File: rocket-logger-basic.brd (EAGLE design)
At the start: 58.5 x 62 mm, 63 parts, among them IC1 CC430F513X, U1 MAX1555, X1 0896BM15A0001, X2 USB-MICROB, X3 SMA-142-0701-801/806

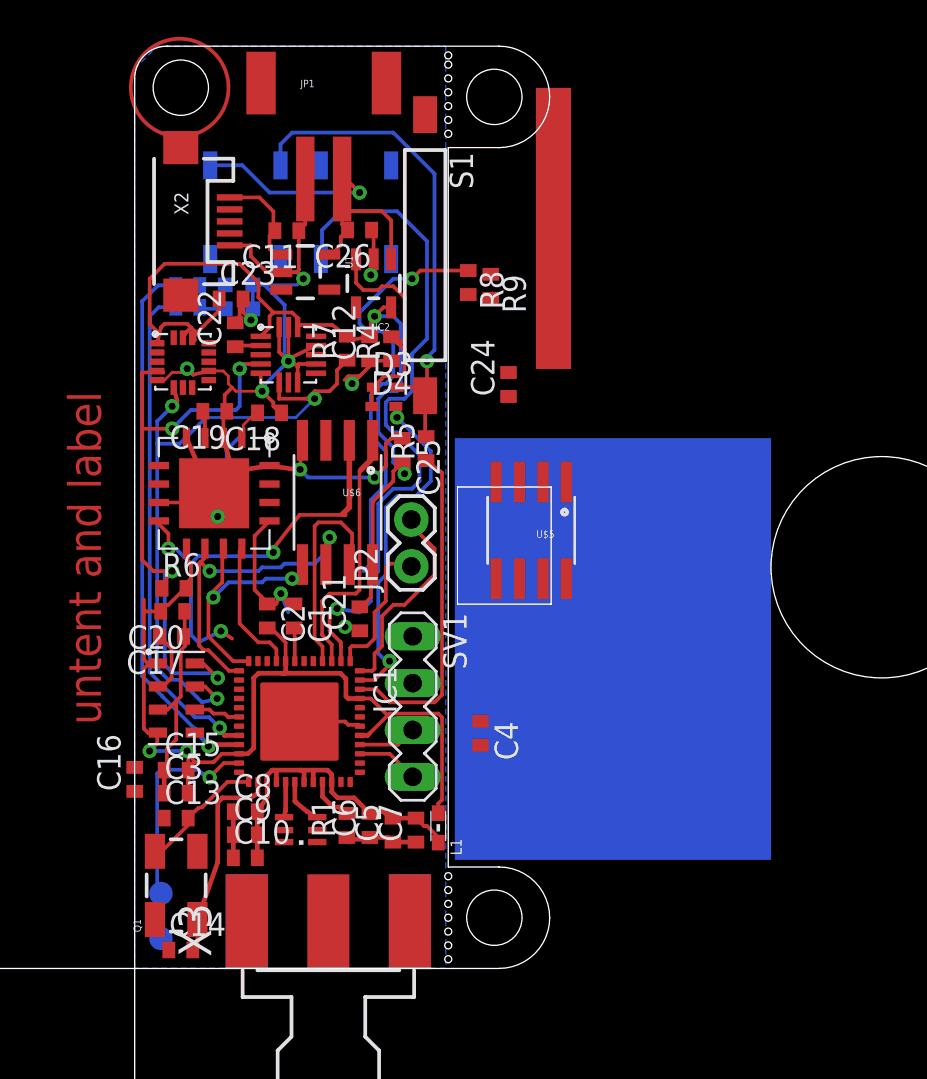
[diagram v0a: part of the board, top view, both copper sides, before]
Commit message: added mini logger
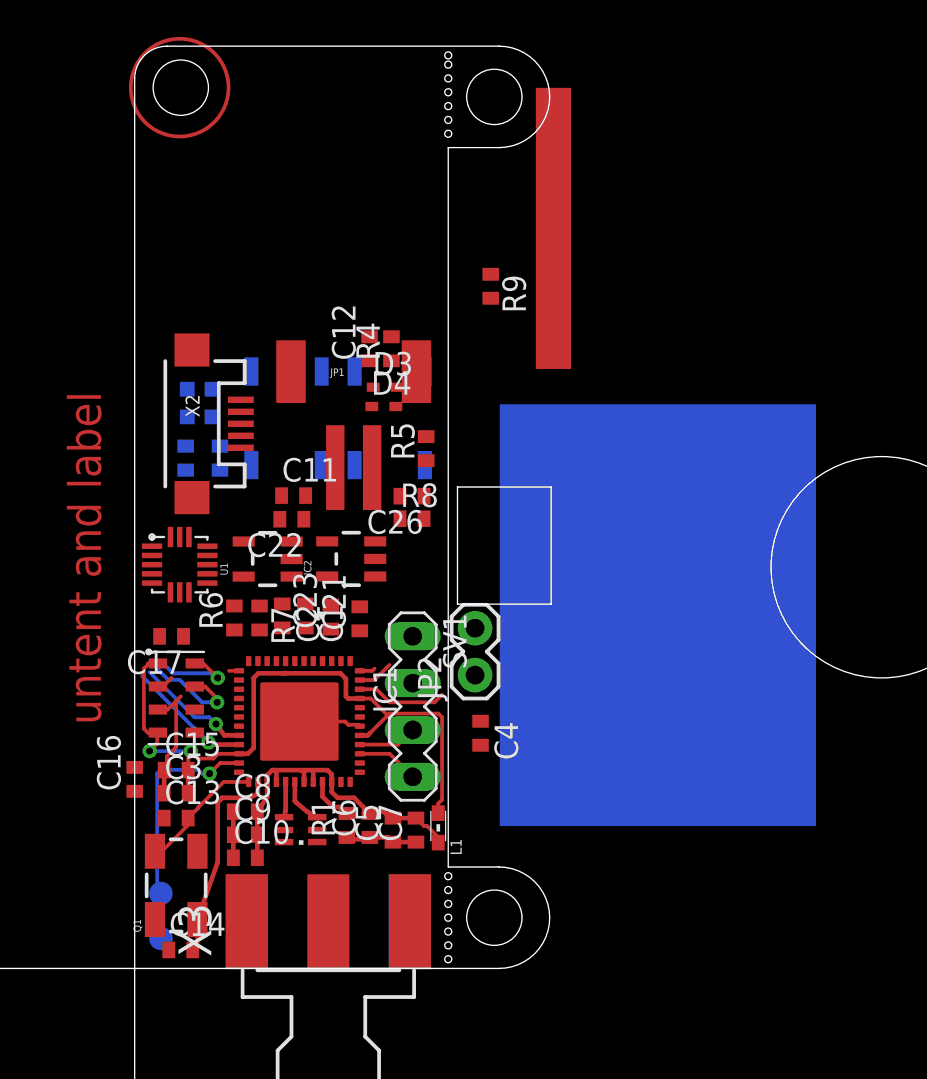
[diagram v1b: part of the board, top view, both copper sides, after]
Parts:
- removed C18, C19: 1u, resistor:C0402
- removed C20: 100n, resistor:C0402
- removed C24, C25: (no value), resistor:C0402
- removed S1: REED-SWITCH-CT10-1530-G1, switch-reed:CT10-G1
- removed U$1: MAX21000, Mine:LGA16
- removed U$2: MMA68XX, Mine:QFN16-6X6
- removed U$5: SPI_FLASH-X25XXSMD, SparkFun:SO08
- removed U$6: SPI_FLASH-X25XXSMD1, SparkFun:SO08-EIAJ
- moved C23 18.1 mm to (10.6, 19.0), turned to 90 degrees
- moved JP1 15.7 mm to (11.9, 30.9)
- moved U1 15.7 mm to (7.21, 22.2), turned to 90 degrees
- moved R7 15.4 mm to (6.77, 19.0), turned to 270 degrees
- moved IC2 15.0 mm to (11.7, 22.2), turned to 90 degrees
- moved C26 14.7 mm to (15.0, 25.6)
- moved C11 14.4 mm to (8.62, 25.6), turned to 0 degrees
- moved R8 13.2 mm to (15.0, 24.4), turned to 0 degrees
- moved U$3 12.8 mm to (2.44, 21.9)
- moved S2 11.4 mm to (8.24, 29.8)
- moved S4 11.3 mm to (13.8, 29.8)
- moved X2 11.0 mm to (3.11, 29.5)
- moved C22 10.5 mm to (8.52, 24.4), turned to 180 degrees
- moved R2 9.53 mm to (4.62, 27.7), turned to 90 degrees
- moved R3 8.18 mm to (2.76, 27.7), turned to 90 degrees
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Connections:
- removed net DSYNC: U$1.12
- removed net N$14: C18.2, U$2.1
- removed net N$15: C19.2, U$2.3
- removed net N$27: U$6.3
- removed net P_INT: IC1.18, U$4.6
- net +3V3: no longer C20.2, C24.2, C25.2, U$1.1, U$1.14, U$1.15, U$2.9, U$6.8
- net CLK: no longer U$2.10, U$6.6
- net CS: no longer U$2.12
- net CS_F: no longer U$6.1
- net GND: no longer C18.1, C19.1, C20.1, C24.1, C25.1, U$1.10, U$1.5, U$1.7, U$2.13, U$2.16, U$2.17, U$2.2, U$2.4, U$2.7, U$3.7, U$6.4
- net HOLD: no longer U$6.7
- net MISO: no longer U$2.8, U$6.2
- net MOSI: no longer U$2.11, U$6.5
- net N$2: no longer S1.1
- net N$24: no longer S1.2
- net SCL: no longer U$1.4
- net SDA: no longer U$1.6
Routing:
- net GND: track 113.1 -> 17.0 mm, vias 12 -> 0
- net +3V3: track 100.6 -> 38.4 mm, vias 4 -> 2
- net N$2: track 43.2 -> 0.00 mm, vias 2 -> 0
- net N$28: track 37.3 -> 0.00 mm, vias 1 -> 0
- net SDA: track 38.0 -> 5.69 mm, vias 3 -> 1
- net SCL: track 34.2 -> 4.88 mm, vias 4 -> 1
- net N$24: track 26.8 -> 0.00 mm, vias 1 -> 0
- net MISO: track 23.9 -> 0.00 mm, vias 3 -> 0
- net N$16: track 29.4 -> 6.79 mm
- net N$17: track 27.2 -> 6.31 mm
- net CLK: track 17.9 -> 0.54 mm, vias 2 -> 0
- net KEEPON: track 19.1 -> 1.95 mm, vias 2 -> 0
- net CS_F: track 14.2 -> 0.00 mm
- net MOSI: track 14.2 -> 0.00 mm, vias 2 -> 0
- net SWITCHON: track 18.0 -> 4.92 mm
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- removed copper zone on layer 16, net GND

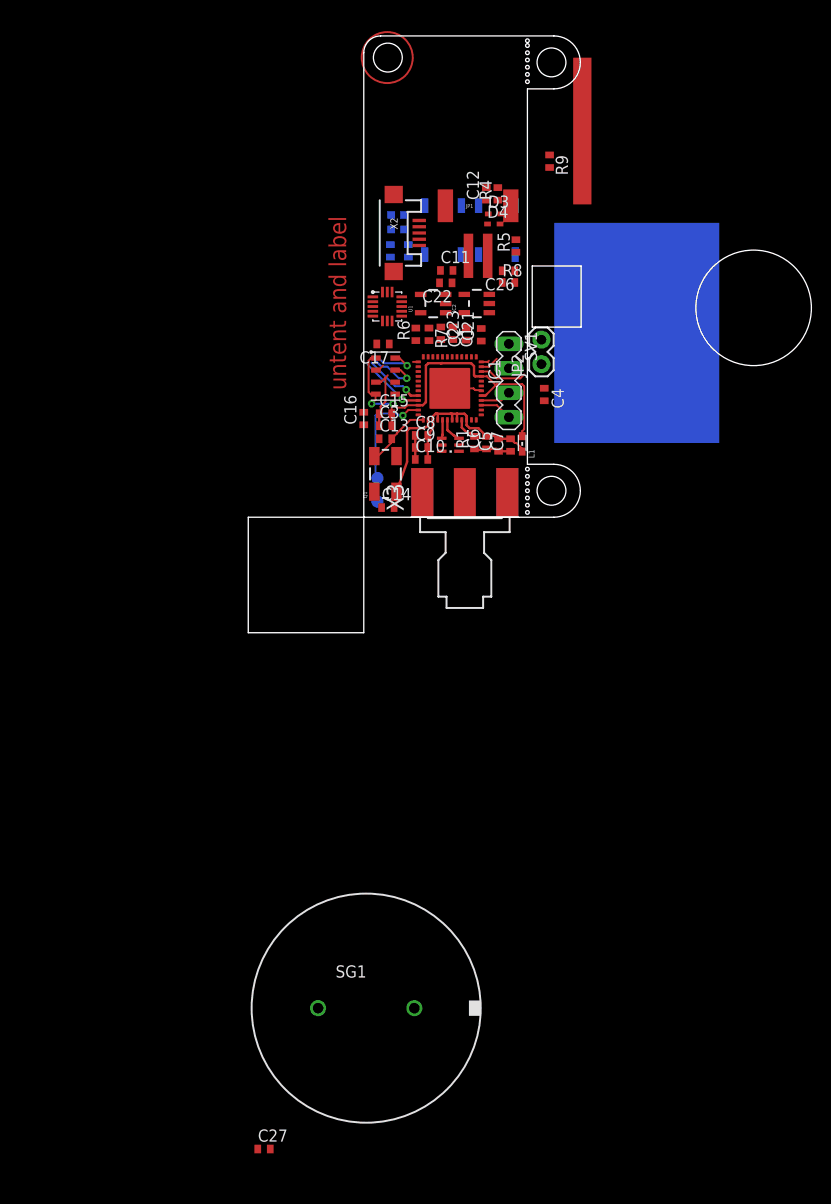
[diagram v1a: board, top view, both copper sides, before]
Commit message: removed accel from simple verison, done some routing on main one
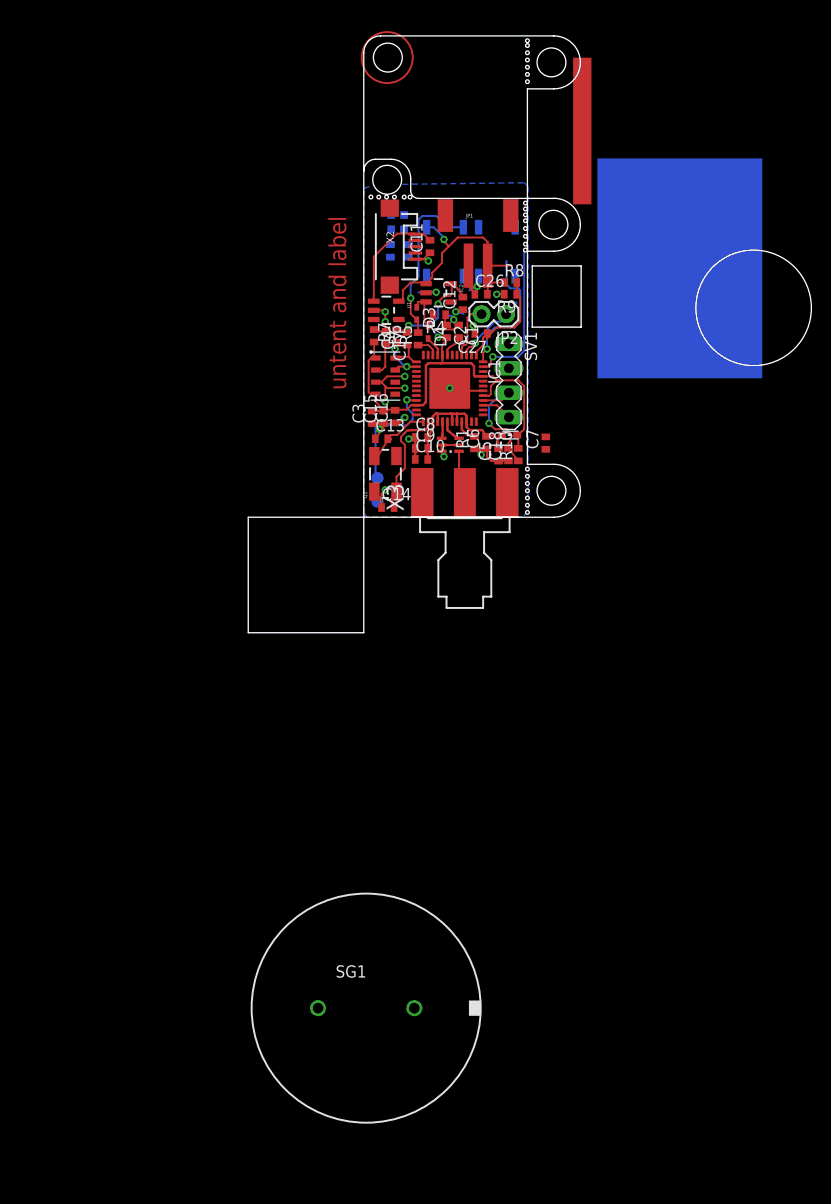
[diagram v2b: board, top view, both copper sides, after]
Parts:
- removed C21: 4.7u, resistor:C0402
- removed C22, C23: 100n, resistor:C0402
- removed U$3: MMA8452Q, Mine:QFN16-COL
- added C18: (no value), resistor:C0402
- added R10: (no value), rcl:R0402
- moved C27 87.7 mm to (12.2, 19.1), turned to 180 degrees
- moved C4 18.7 mm to (1.07, 18.8)
- moved R9 14.4 mm to (15.2, 23.2), turned to 180 degrees
- moved R5 14.0 mm to (5.64, 18.5)
- moved R4 13.9 mm to (7.86, 21.0), turned to 180 degrees
- moved D4 13.1 mm to (6.69, 19.3), turned to 270 degrees
- moved D3 13.1 mm to (5.50, 21.2), turned to 270 degrees
- moved C12 11.6 mm to (10.3, 22.2)
- moved JP2 6.36 mm to (14.8, 21.1), turned to 180 degrees
- moved U1 4.92 mm to (2.34, 21.5), turned to 270 degrees
- moved IC2 4.13 mm to (7.77, 23.3), turned to 270 degrees
- moved C26 3.75 mm to (12.2, 23.2), turned to 0 degrees
- moved C7 3.66 mm to (18.9, 7.70)
- moved R7 3.39 mm to (3.39, 18.8), turned to 90 degrees
- moved C16 3.26 mm to (3.25, 10.5)
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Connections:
- removed net CLK: IC1.13
- removed net CS: IC1.9
- removed net CS_F: IC1.3
- removed net HOLD: IC1.4
- removed net MISO: IC1.14
- removed net MOSI: IC1.12
- removed net N$19: C22.1, U$3.2
- removed net N$28: IC1.2, S4.3
- net +3V3: now also R10.2; no longer C21.2, C23.1, U$3.1, U$3.14
- net GND: now also C18.1; no longer C21.1, C22.2, C23.2, U$3.10, U$3.12, U$3.13, U$3.15, U$3.16, U$3.5, U$3.8
- net KEEPON: now also IC1.9; no longer IC1.47
- net N$11: now also IC1.3; no longer IC1.1
- net N$12: now also IC1.4; no longer IC1.48
- net N$16: now also IC1.48; no longer IC1.21
- net N$17: now also IC1.47; no longer IC1.20
- net N$26: now also C18.2, R10.1
- net N$29: now also IC1.21; no longer IC1.23
- net SCL: now also IC1.13; no longer IC1.11, U$3.4
- net SDA: now also IC1.14; no longer IC1.10, U$3.6
- net SWITCHON: now also IC1.10; no longer IC1.46
- net VBAT: now also IC1.1
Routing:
- net GND: track 17.0 -> 59.3 mm, vias 0 -> 19
- net N$2: track 0.00 -> 26.7 mm, vias 0 -> 1
- net +3V3: track 38.4 -> 59.3 mm, vias 2 -> 3
- net N$24: track 0.00 -> 18.1 mm, vias 0 -> 1
- net VBAT: track 0.00 -> 11.9 mm
- net N$1: track 0.00 -> 11.7 mm
- net N$26: track 3.19 -> 13.4 mm, vias 0 -> 1
- net N$17: track 6.31 -> 16.2 mm
- net N$16: track 6.79 -> 14.1 mm
- net N$25: track 0.00 -> 6.57 mm
- net N$11: track 0.00 -> 6.36 mm, vias 0 -> 1
- net N$12: track 0.98 -> 5.86 mm
- net N$8: track 0.00 -> 4.53 mm
- net SWITCHON: track 4.92 -> 2.29 mm
- net N$13: track 0.93 -> 3.53 mm
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- added copper zone on layer 16, net GND
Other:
- outline, holes or cut-outs redrawn

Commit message: added charging led
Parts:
- removed S4: SWITCH-MOMENTARY-2SMD, SparkFun:TACTILE_SWITCH_SMD
- removed SV1: (no value), con-lstb:MA04-1
- added JP3: (no value), SparkFun:1X04
- added LED3: (no value), SparkFun:LED-0603
- added R11: (no value), rcl:R0402
- moved R3 11.2 mm to (13.7, 25.2)
- moved LED1 11.1 mm to (15.0, 27.8)
- moved LED2 11.1 mm to (13.6, 27.8)
- moved R2 10.6 mm to (15.0, 25.2)
- moved JP2 0.20 mm to (15.0, 21.1)
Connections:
- new net INT2: IC1.17, U$4.6
- new net N$15: R11.1, U1.3
- new net N$18: LED3.C, R11.2
- net +3V3: now also JP3.1
- net GND: now also JP3.2
- net N$1: now also LED3.A
- net N$23: now also JP3.4; no longer SV1.4
- net N$26: now also JP3.3; no longer SV1.3
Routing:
- net +3V3: track 59.3 -> 64.3 mm
- net GND: track 59.3 -> 56.6 mm, vias 19 -> 18
- net INT2: track 0.00 -> 2.33 mm
- net N$16: track 14.1 -> 12.3 mm

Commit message: done some routing
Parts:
- added D1: (no value), diode:SOD523
- added IC3: (no value), SparkFun:SOT23-5
- added Q2: MOSFET-PCHANNEL, SparkFun:SOT23
- added R12: (no value), rcl:R0402
- added U2: MAX1555, SparkFun:SOT23-5
- moved LED3 101.1 mm to (12.4, 27.8), flipped to the bottom
- moved R11 98.0 mm to (12.4, 25.2), flipped to the bottom, turned to 270 degrees
- moved R4 10.6 mm to (17.8, 17.2), turned to 90 degrees
- moved U1 6.22 mm to (8.49, 22.4), turned to 180 degrees
- moved D4 4.60 mm to (2.69, 21.5), turned to 0 degrees
- moved C12 4.19 mm to (6.84, 19.8), turned to 180 degrees
- moved R5 3.64 mm to (2.60, 20.5), turned to 180 degrees
- moved D3 3.08 mm to (2.72, 22.5), turned to 180 degrees
- moved IC2 2.47 mm to (5.43, 22.5), turned to 180 degrees
- moved C11 1.83 mm to (6.88, 26.3)
- moved C26 1.59 mm to (10.8, 22.5), turned to 90 degrees
- moved R7 0.39 mm to (3.03, 18.6)
- moved R6 0.37 mm to (4.13, 18.6)
- moved C17 0.36 mm to (1.96, 18.7)
- moved C4 0.29 mm to (0.87, 18.6)
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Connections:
- removed net N$1: C11.2, LED3.A, U1.1, X2.VBUS
- new net N$19: LED3.C, U1.3
- new net N$20: D1.C, IC3.1, Q2.3
- new net N$21: D1.A, Q2.1, R12.1, U2.1
- new net N$22: R12.2
- new net N$27: Q2.2, U2.5
- net KEEPON: now also IC1.11; no longer IC1.9
- net N$15: now also LED3.A; no longer U1.3
- net N$18: now also C11.2, U1.1, X2.VBUS; no longer LED3.C
- net N$25: no longer R4.2
- net SWITCHON: now also IC1.12; no longer IC1.10
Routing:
- net N$19: track 0.00 -> 18.9 mm, vias 0 -> 1
- net N$18: track 0.00 -> 15.6 mm, vias 0 -> 1
- net N$1: track 11.7 -> 0.00 mm
- net KEEPON: track 2.20 -> 8.05 mm
- net SWITCHON: track 2.29 -> 5.49 mm
- net GND: track 56.6 -> 54.0 mm
- net N$25: track 6.57 -> 4.23 mm
- net +3V3: track 64.3 -> 62.3 mm, vias 3 -> 2
- net N$24: track 18.1 -> 19.9 mm
- net N$10: track 0.00 -> 1.30 mm
- net N$15: track 0.00 -> 1.24 mm
- net N$9: track 0.00 -> 1.20 mm
